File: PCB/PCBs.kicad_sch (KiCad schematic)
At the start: 52 parts, among them CN1 W2A41C681KAT2A, CN2 W2A41C681KAT2A, CN3 W2A41C681KAT2A, CN6 W2A41C681KAT2A, U1 ADS1299IPAGR, U10 TPD4E1B06DCKR, U11 TPS61023DRLR, U3 TPD4E1B06DCKR, U4 TPD4E1B06DCKR, U5 TPS73225DBVR, U7 LM2664M6, U8 TPS73233DBVT, U9 TPS72325DBVT

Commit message: avss adjustments
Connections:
- net +3V3: now also R1.1, U1.48 (DVDD)
- net -2V5: now also U1.17 (SRB1), U1.18 (SRB2), U1.60 (BIASREF)
- no-connect marks 7 -> 4
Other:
- note added: "EEG Shield for Raspberry Pi Pico W"
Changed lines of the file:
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@@
 	)
 	(junction
-		(at 29.21 110.49)
-		(diameter 0)
-		(color 0 0 0 0)
-	)
-	(junction
 		(at 146.05 40.64)
 		(diameter 0)
@@
 	)
 	(junction
+		(at 22.86 118.11)
+		(diameter 0)
+		(color 0 0 0 0)
+	)
+	(junction
 		(at 57.15 135.89)
 		(diameter 0)
@@
 	)
 	(junction
+		(at 240.03 81.28)
+		(diameter 0)
+		(color 0 0 0 0)
+	)
+	(junction
 		(at 62.23 52.07)
 		(diameter 0)
@@
 	)
 	(junction
+		(at 29.21 110.49)
+		(diameter 0)
+		(color 0 0 0 0)
+	)
+	(junction
 		(at 129.54 44.45)
 		(diameter 0)
@@
 	)
 	(junction
+		(at 185.42 140.97)
+		(diameter 0)
+		(color 0 0 0 0)
+	)
+	(junction
 		(at 222.25 67.31)
 		(diameter 0)
@@
 	)
 	(junction
+		(at 240.03 78.74)
+		(diameter 0)
+		(color 0 0 0 0)
+	)
+	(junction
 		(at 22.86 163.83)
 		(diameter 0)
@@
 	)
 	(junction
+		(at 182.88 140.97)
+		(diameter 0)
+		(color 0 0 0 0)
+	)
+	(junction
 		(at 179.07 67.31)
 		(diameter 0)
@@
 	)
 	(no_connect
-		(at 189.23 67.31)
-	)
-	(no_connect
 		(at 240.03 124.46)
 	)
 	(no_connect
-		(at 182.88 138.43)
-	)
-	(no_connect
 		(at 240.03 119.38)
 	)
 	(no_connect
-		(at 185.42 138.43)
-	)
-	(no_connect
 		(at 240.03 116.84)
 	)
@@
 	(wire
 		(pts
-			(xy 177.8 142.24) (xy 177.8 157.48)
+			(xy 177.8 140.97) (xy 177.8 157.48)
 		)
 		(stroke
@@
 	(wire
 		(pts
+			(xy 189.23 67.31) (xy 194.31 67.31)
+		)
+		(stroke
+			(width 0)
+			(type default)
+		)
+	)
+	(wire
+		(pts
 			(xy 215.9 138.43) (xy 218.44 138.43)
 		)
@@
 	(wire
 		(pts
-			(xy 17.78 125.73) (xy 30.48 125.73)
-		)
-		(stroke
-			(width 0)
-			(type default)
-		)
-	)
-	(wire
-		(pts
 			(xy 93.98 33.02) (xy 97.79 33.02)
 		)
@@
 	(wire
 		(pts
-			(xy 177.8 142.24) (xy 191.77 142.24)
+			(xy 177.8 140.97) (xy 182.88 140.97)
+		)
+		(stroke
+			(width 0)
+			(type default)
+		)
+	)
+	(wire
+		(pts
+			(xy 182.88 140.97) (xy 182.88 142.24)
 		)
 		(stroke
@@
 	(wire
 		(pts
+			(xy 22.86 125.73) (xy 22.86 118.11)
+		)
+		(stroke
+			(width 0)
+			(type default)
+		)
+	)
+	(wire
+		(pts
 			(xy 161.29 88.9) (xy 168.91 88.9)
 		)
@@
 	(wire
 		(pts
-			(xy 191.77 138.43) (xy 191.77 142.24)
+			(xy 191.77 138.43) (xy 191.77 140.97)
 		)
 		(stroke
@@
 	(wire
 		(pts
+			(xy 22.86 110.49) (xy 29.21 110.49)
+		)
+		(stroke
+			(width 0)
+			(type default)
+		)
+	)
+	(wire
+		(pts
 			(xy 104.14 25.4) (xy 104.14 33.02)
 		)
@@
 	(wire
 		(pts
+			(xy 17.78 118.11) (xy 22.86 118.11)
+		)
+		(stroke
+			(width 0)
+			(type default)
+		)
+	)
+	(wire
+		(pts
 			(xy 143.51 40.64) (xy 143.51 44.45)
 		)
@@
 	(wire
 		(pts
+			(xy 240.03 78.74) (xy 240.03 81.28)
+		)
+		(stroke
+			(width 0)
+			(type default)
+		)
+	)
+	(wire
+		(pts
 			(xy 124.46 25.4) (xy 124.46 33.02)
 		)
@@
 	(wire
 		(pts
+			(xy 182.88 140.97) (xy 185.42 140.97)
+		)
+		(stroke
+			(width 0)
+			(type default)
+		)
+	)
+	(wire
+		(pts
 			(xy 34.29 29.21) (xy 36.83 29.21)
 		)
@@
 	(wire
 		(pts
+			(xy 182.88 138.43) (xy 182.88 140.97)
+		)
+		(stroke
+			(width 0)
+			(type default)
+		)
+	)
+	(wire
+		(pts
 			(xy 38.1 87.63) (xy 29.21 87.63)
 		)
@@
 	(wire
 		(pts
+			(xy 185.42 140.97) (xy 191.77 140.97)
+		)
+		(stroke
+			(width 0)
+			(type default)
+		)
+	)
+	(wire
+		(pts
 			(xy 212.09 157.48) (xy 218.44 157.48)
 		)
@@
 	(wire
 		(pts
+			(xy 30.48 125.73) (xy 22.86 125.73)
+		)
+		(stroke
+			(width 0)
+			(type default)
+		)
+	)
+	(wire
+		(pts
 			(xy 161.29 116.84) (xy 168.91 116.84)
 		)
@@
 	(wire
 		(pts
-			(xy 17.78 110.49) (xy 29.21 110.49)
-		)
-		(stroke
-			(width 0)
-			(type default)
-		)
-	)
-	(wire
-		(pts
 			(xy 182.88 149.86) (xy 182.88 143.51)
 		)
@@
 	(wire
 		(pts
+			(xy 22.86 118.11) (xy 22.86 110.49)
+		)
+		(stroke
+			(width 0)
+			(type default)
+		)
+	)
+	(wire
+		(pts
 			(xy 57.15 135.89) (xy 57.15 142.24)
 		)
@@
 	(wire
 		(pts
+			(xy 185.42 138.43) (xy 185.42 140.97)
+		)
+		(stroke
+			(width 0)
+			(type default)
+		)
+	)
+	(wire
+		(pts
 			(xy 196.85 52.07) (xy 199.39 52.07)
 		)
@@
 		)
 	)
+	(text "EEG Shield for Raspberry Pi Pico W"
+		(exclude_from_sim no)
+		(at 203.962 189.992 0)
+		(effects
+			(font
+				(size 1.27 1.27)
+			)
+		)
+	)
 	(text "1nF"
 		(exclude_from_sim no)
@@
 		)
 	)
-	(label "I4"
-		(at 17.78 125.73 0)
-		(fields_autoplaced yes)
-		(effects
-			(font
-				(size 1.27 1.27)
-			)
-			(justify left bottom)
-		)
-	)
 	(label "IN6N"
 		(at 161.29 96.52 0)
@@
 	)
 	(label "I4"
-		(at 17.78 110.49 0)
+		(at 17.78 118.11 0)
 		(fields_autoplaced yes)
 		(effects
@@
 				)
 				(justify right)
+				(hide yes)
 			)
 		)

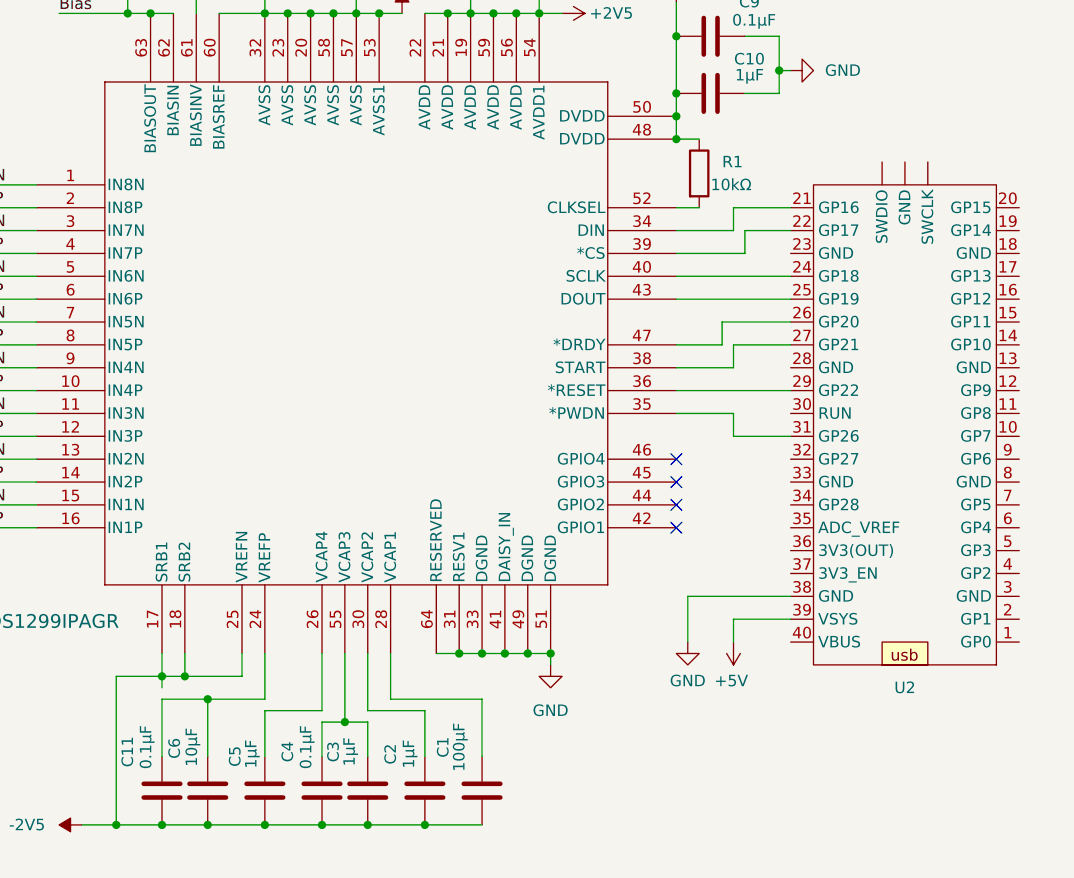
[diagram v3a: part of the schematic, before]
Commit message: ground unused gpio
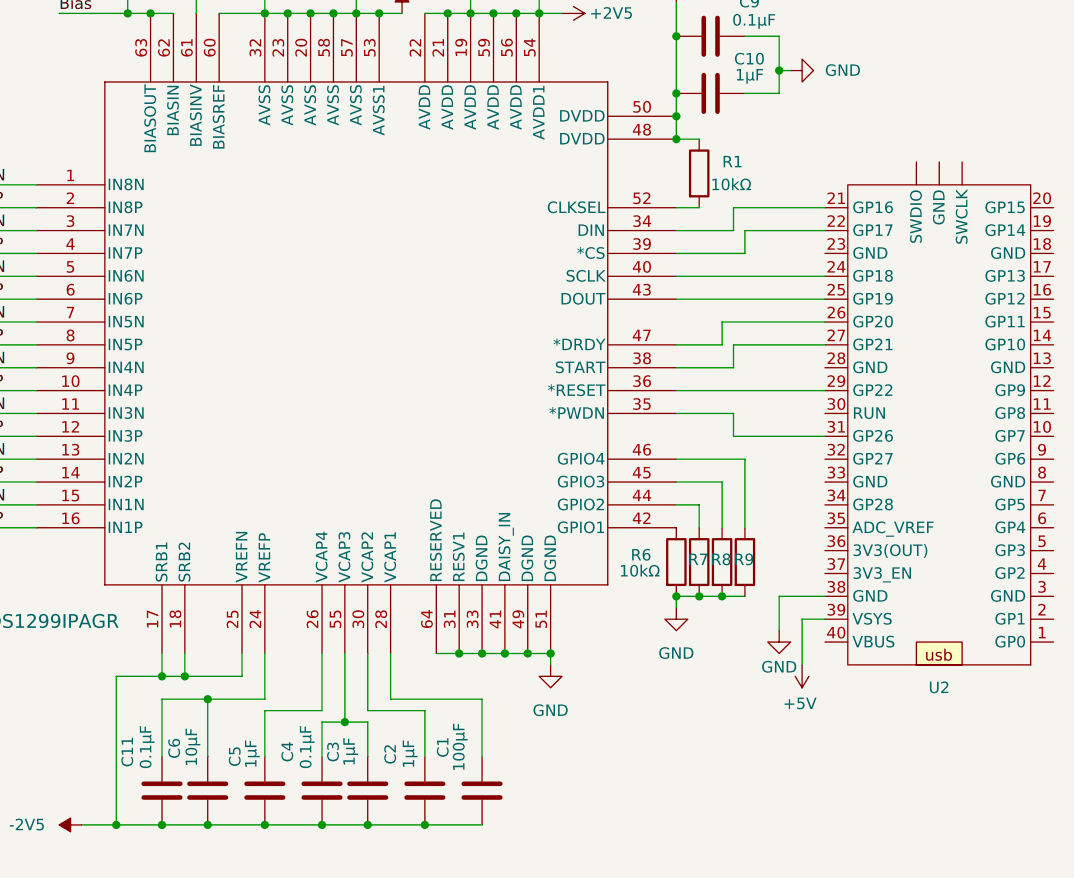
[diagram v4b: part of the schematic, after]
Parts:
- added R6, R7, R8, R9: 10kΩ, symbol Device:R
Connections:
- net GND: now also R6.2, R7.2, R8.2, R9.2
- net at U1.42 (GPIO1): now also R6.1
- net at U1.44 (GPIO2): now also R7.1
- net at U1.45 (GPIO3): now also R8.1
- net at U1.46 (GPIO4): now also R9.1
- no-connect marks 4 -> 0
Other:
- moved on the sheet: U2

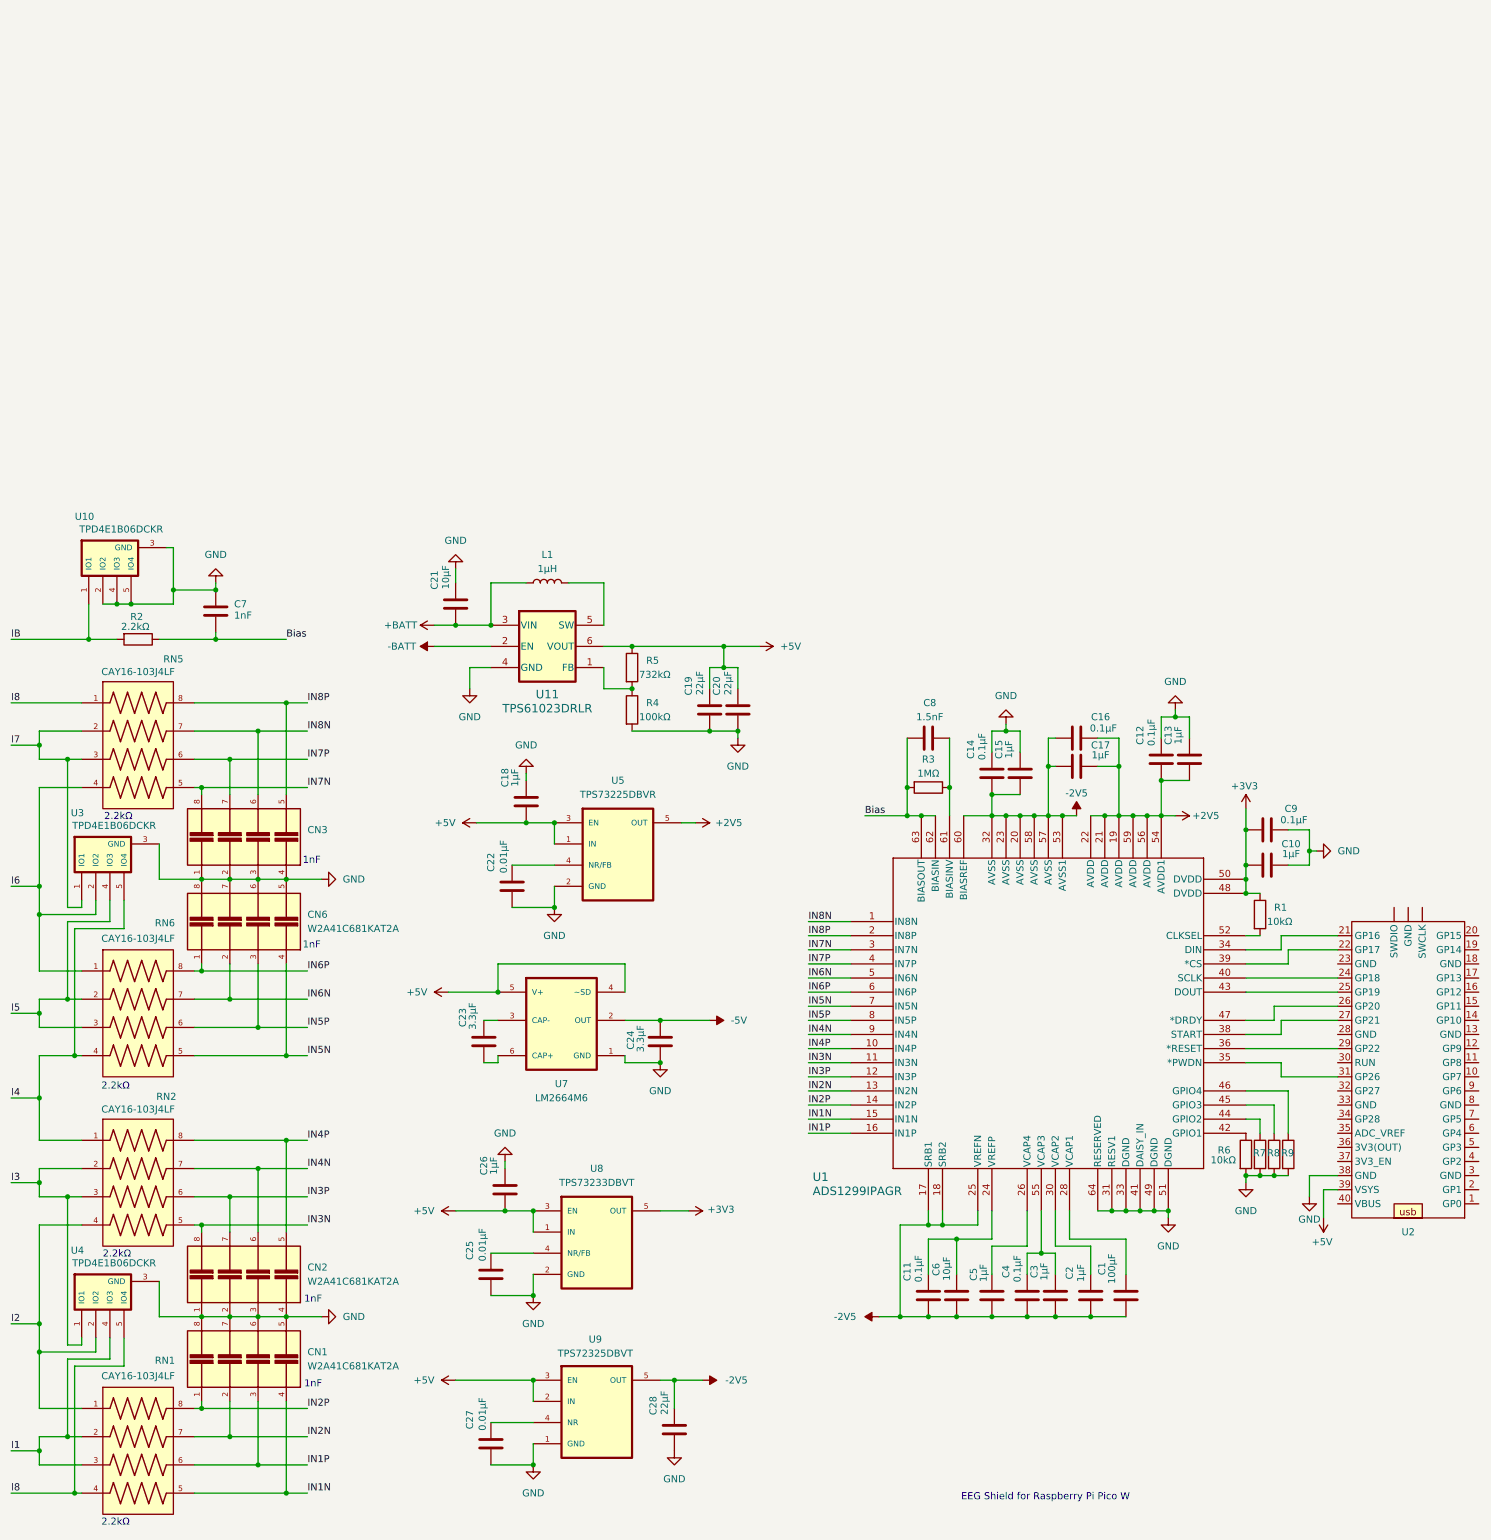
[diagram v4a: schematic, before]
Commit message: simplifying inputs
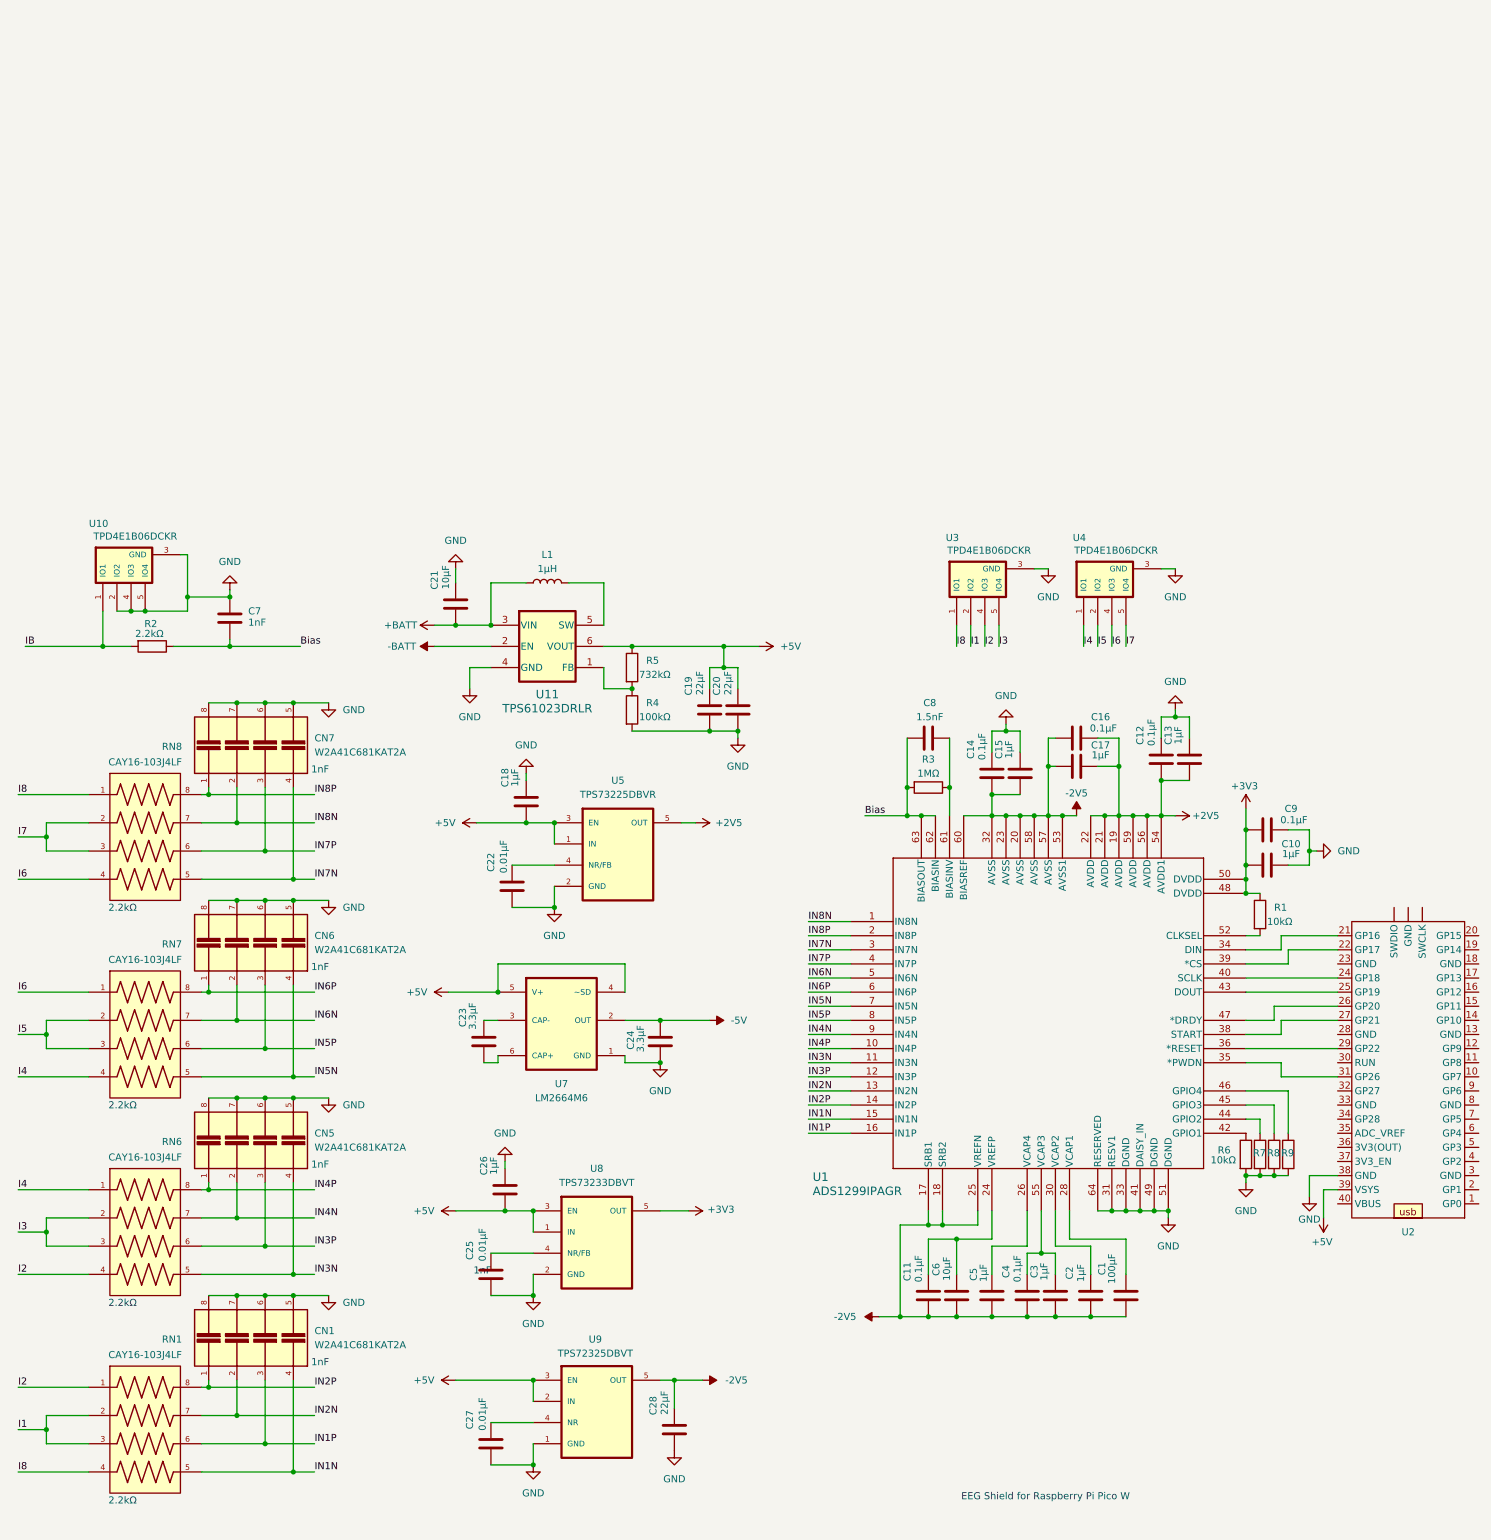
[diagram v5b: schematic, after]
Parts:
- removed CN2, CN3: W2A41C681KAT2A, W2A41C681KAT2A:CAPCAXE50P210X130X94-8N, symbol custom_lib:W2A41C681KAT2A
- removed RN2, RN5: CAY16-103J4LF, CAY16-103J4LF:RESCAF80P320X160X60-8N, symbol custom_lib:CAY16-103J4LF
- added CN5, CN7: W2A41C681KAT2A, W2A41C681KAT2A:CAPCAXE50P210X130X94-8N, symbol custom_lib:W2A41C681KAT2A
- added RN7, RN8: CAY16-103J4LF, CAY16-103J4LF:RESCAF80P320X160X60-8N, symbol custom_lib:CAY16-103J4LF
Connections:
- net GND: now also CN5.5, CN5.6, CN5.7, CN5.8, CN7.5, CN7.6, CN7.7, CN7.8
- net I1: now also U3.2 (IO2); no longer U4.4 (IO3)
- net I2: now also RN6.4, U3.4 (IO3); no longer U4.2 (IO2)
- net I3: now also RN6.2, RN6.3, U3.5 (IO4); no longer U4.1 (IO1)
- net I4: now also RN6.1, U4.1 (IO1), RN7.4; no longer RN6.4, U3.5 (IO4)
- net I5: now also U4.2 (IO2), RN7.2, RN7.3; no longer RN6.2, RN6.3, U3.4 (IO3)
- net I6: now also U4.4 (IO3), RN7.1, RN8.4; no longer RN6.1, U3.2 (IO2)
- net I7: now also U4.5 (IO4), RN8.2, RN8.3; no longer U3.1 (IO1)
- net I8: now also U3.1 (IO1), RN8.1; no longer U4.5 (IO4)
- net IN3N: now also RN6.5, CN5.4
- net IN3P: now also RN6.6, CN5.3
- net IN4N: now also RN6.7, CN5.2
- net IN4P: now also RN6.8, CN5.1
- net IN5N: now also RN7.5; no longer RN6.5
- net IN5P: now also RN7.6; no longer RN6.6
- net IN6N: now also RN7.7; no longer RN6.7
- net IN6P: now also RN7.8; no longer RN6.8
- net IN7N: now also CN7.4, RN8.5
- net IN7P: now also CN7.3, RN8.6
- net IN8N: now also CN7.2, RN8.7
- net IN8P: now also CN7.1, RN8.8
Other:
- moved on the sheet: C7, CN1, R2, RN1, U10
